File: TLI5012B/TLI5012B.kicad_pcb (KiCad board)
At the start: 2 copper layers, 13.2 x 13.2 mm, 7 parts, among them J1 Conn_01x05_Female, U1 TLI5012B

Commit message: with pcb for walkera_wk-ws-028-014A
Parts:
- removed D1: LED, LED_SMD:LED_0603_1608Metric
- removed G***: LOGO, custom_lib:R1_eyes_mask_5.5mm
- removed G***: LOGO, custom_lib:R1_face_mask_5.5mm
- removed G***: LOGO, custom_lib:R1_ear_silk_5.5mm
- removed R1: 1k, LED_SMD:LED_0402_1005Metric
- added C1: C, Capacitor_SMD:C_0402_1005Metric, B.Cu at (136.7, 86.4)
- added H1: MountingHole, MountingHole:MountingHole_3.2mm_M3, F.Cu at (137.8, 93.7)
- added H2: MountingHole, MountingHole:MountingHole_3.2mm_M3, F.Cu at (137.8, 79.0)
- added H3: MountingHole, MountingHole:MountingHole_3.2mm_M3, F.Cu at (130.4, 86.4)
- added H4: MountingHole, MountingHole:MountingHole_3.2mm_M3, F.Cu at (145.1, 86.4)
- J1: footprint Connector_JST:JST_SH_SM05B-SRSS-TB_1x05-1MP_P1.00mm_Horizontal -> Connector_PinHeader_2.54mm:PinHeader_1x05_P2.54mm_Vertical; moved to F.Cu
- U1: footprint Package_SO:SO-8_5.3x6.2mm_P1.27mm -> custom_lib:TLI5012B
- moved J1 15.2 mm to (133.9, 98.1), turned to 225 degrees
- moved U1 0.14 mm to (137.8, 86.4), turned to 90 degrees
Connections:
- J1 pad 1: /IFB -> /IFC
- J1 pad 2: /IFA -> /IFB
- J1 pad 3: /IFC -> /IFA
- J1 pad 4: /GND -> GND
- J1 pad 5: /VDD -> +5V
- U1 pad 6: /VDD -> +5V
- U1 pad 7: /GND -> GND
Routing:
- net +5V: track 0.00 -> 13.6 mm, vias 0 -> 1
- net /GND: track 11.2 -> 0.00 mm, vias 2 -> 0
- net /IFC: track 5.17 -> 14.9 mm, vias 1 -> 0
- net /VDD: track 4.24 -> 0.00 mm, vias 1 -> 0
- net /IFA: track 17.5 -> 14.7 mm
- net GND: track 0.00 -> 1.78 mm, vias 0 -> 1
- net Net-(D1-Pad2): track 1.56 -> 0.00 mm
- net /IFB: track 10.2 -> 9.23 mm, vias 1 -> 0
- added copper zone on F.Cu, net GND
- removed copper zone on F.Cu, net +5V
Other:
- board size 13.2 x 13.2 mm -> 24.2 x 24.9 mm
- board text added: "100n"
- board text added: "5V"
- board text added: "A"
- board text added: "B"
- board text added: "GND"
- board text added: "I"
- board text added: "TLI5012B"

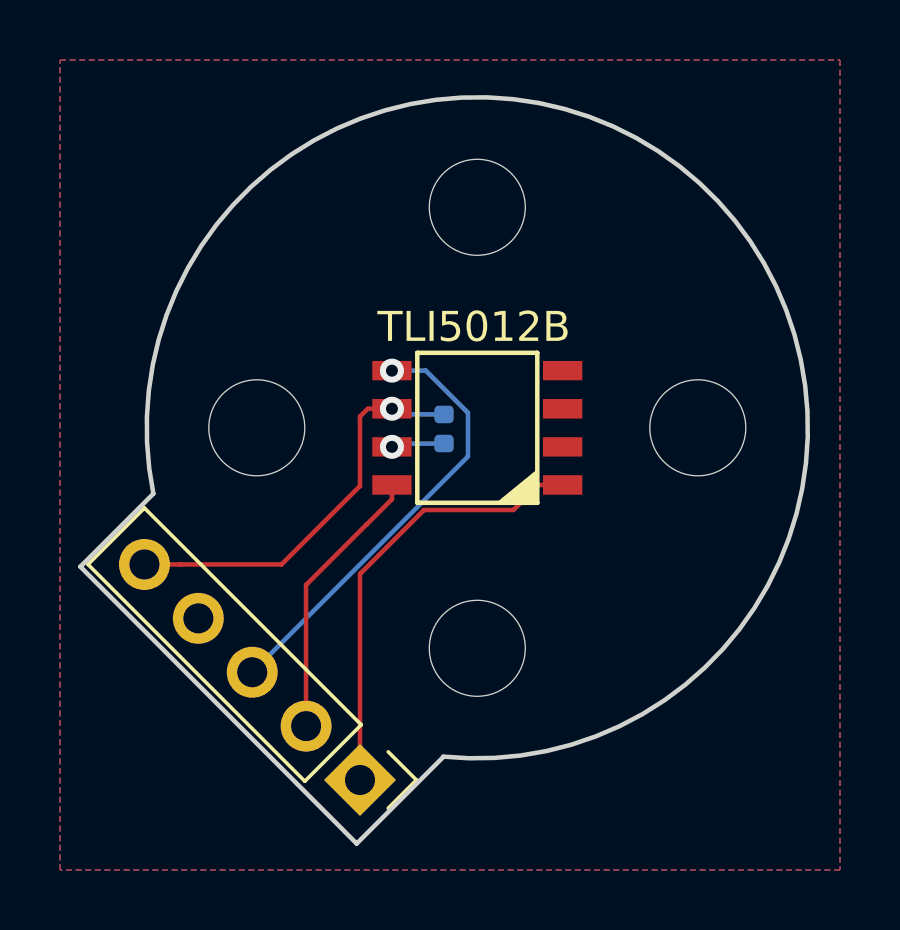
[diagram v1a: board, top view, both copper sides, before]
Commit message: with 1.27 pitch
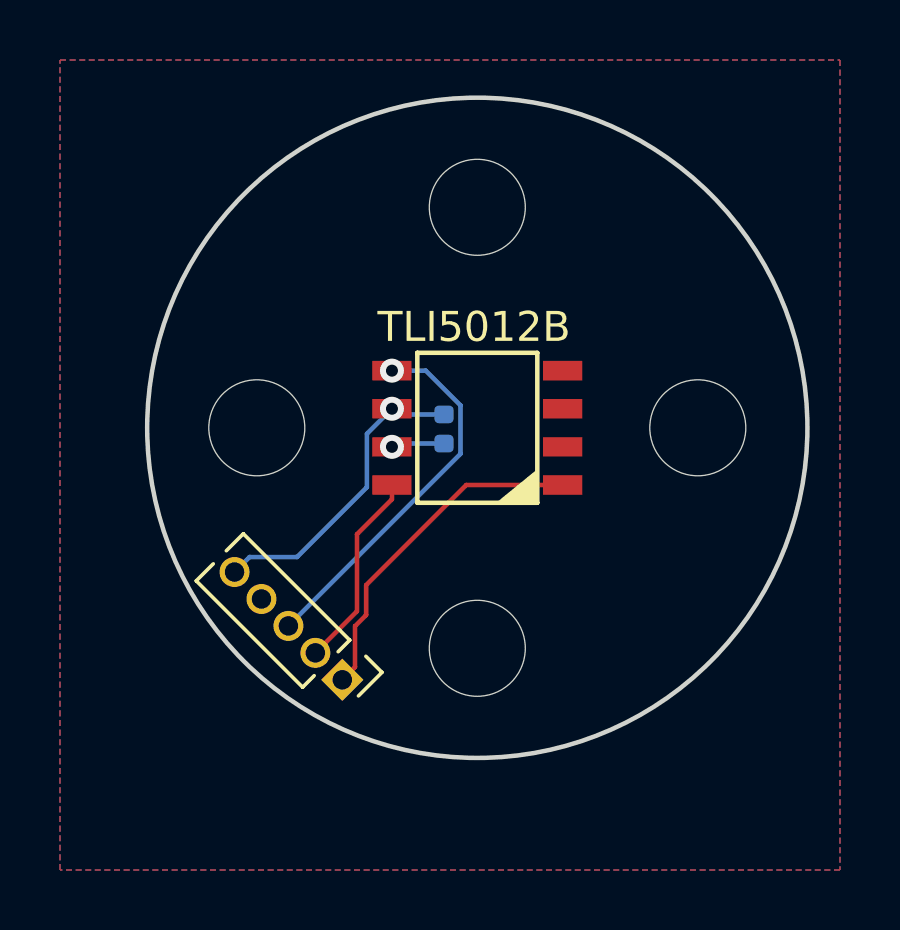
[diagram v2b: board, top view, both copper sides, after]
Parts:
- J1: footprint Connector_PinHeader_2.54mm:PinHeader_1x05_P2.54mm_Vertical -> Connector_PinHeader_1.27mm:PinHeader_1x05_P1.27mm_Vertical
- moved J1 3.39 mm to (133.3, 94.8)
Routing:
- net /IFC: track 14.9 -> 11.4 mm
- net +5V: track 13.6 -> 10.4 mm
- net /IFB: track 9.23 -> 6.65 mm
- net /IFA: track 14.7 -> 12.5 mm
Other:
- board size 24.2 x 24.9 mm -> 22 x 22 mm
